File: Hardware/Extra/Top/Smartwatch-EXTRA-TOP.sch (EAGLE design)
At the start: 72 parts, among them U1 NRF52832_MODULE_MDBT42, U3 FT231XS, U4 PHOTOTRANSISTOR, U5 MCP9808-MSOP8

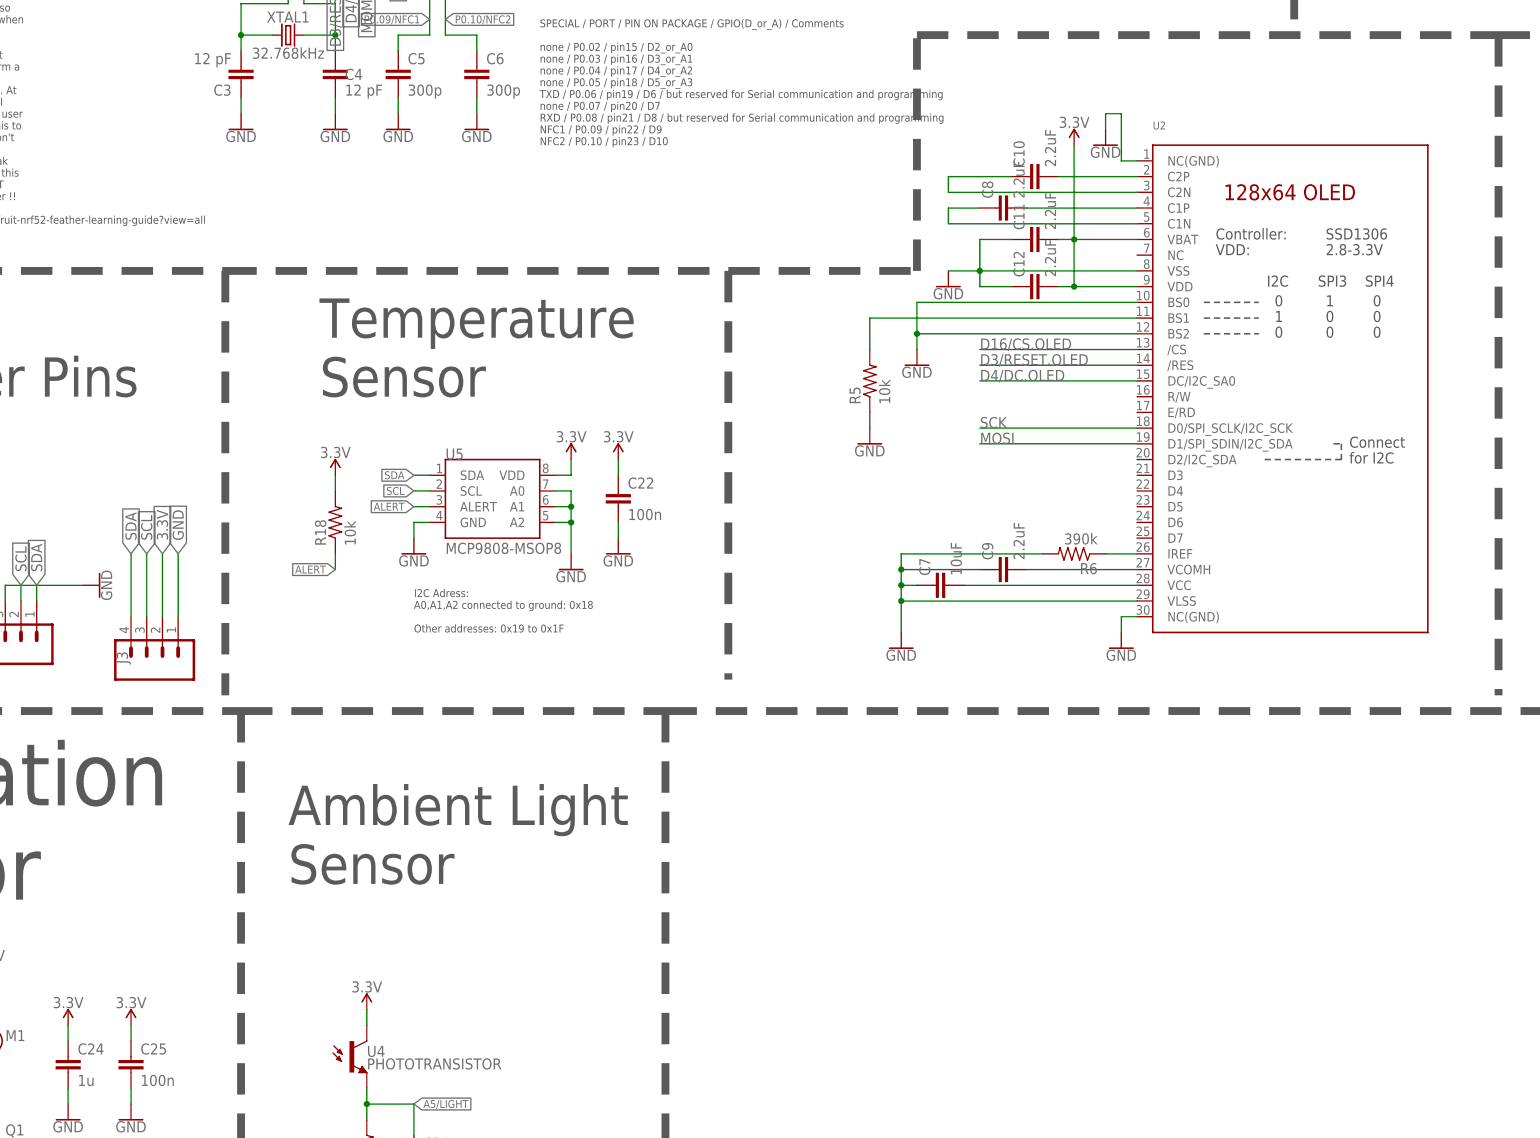
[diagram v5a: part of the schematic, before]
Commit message: Removed GPS, rearranged some other components
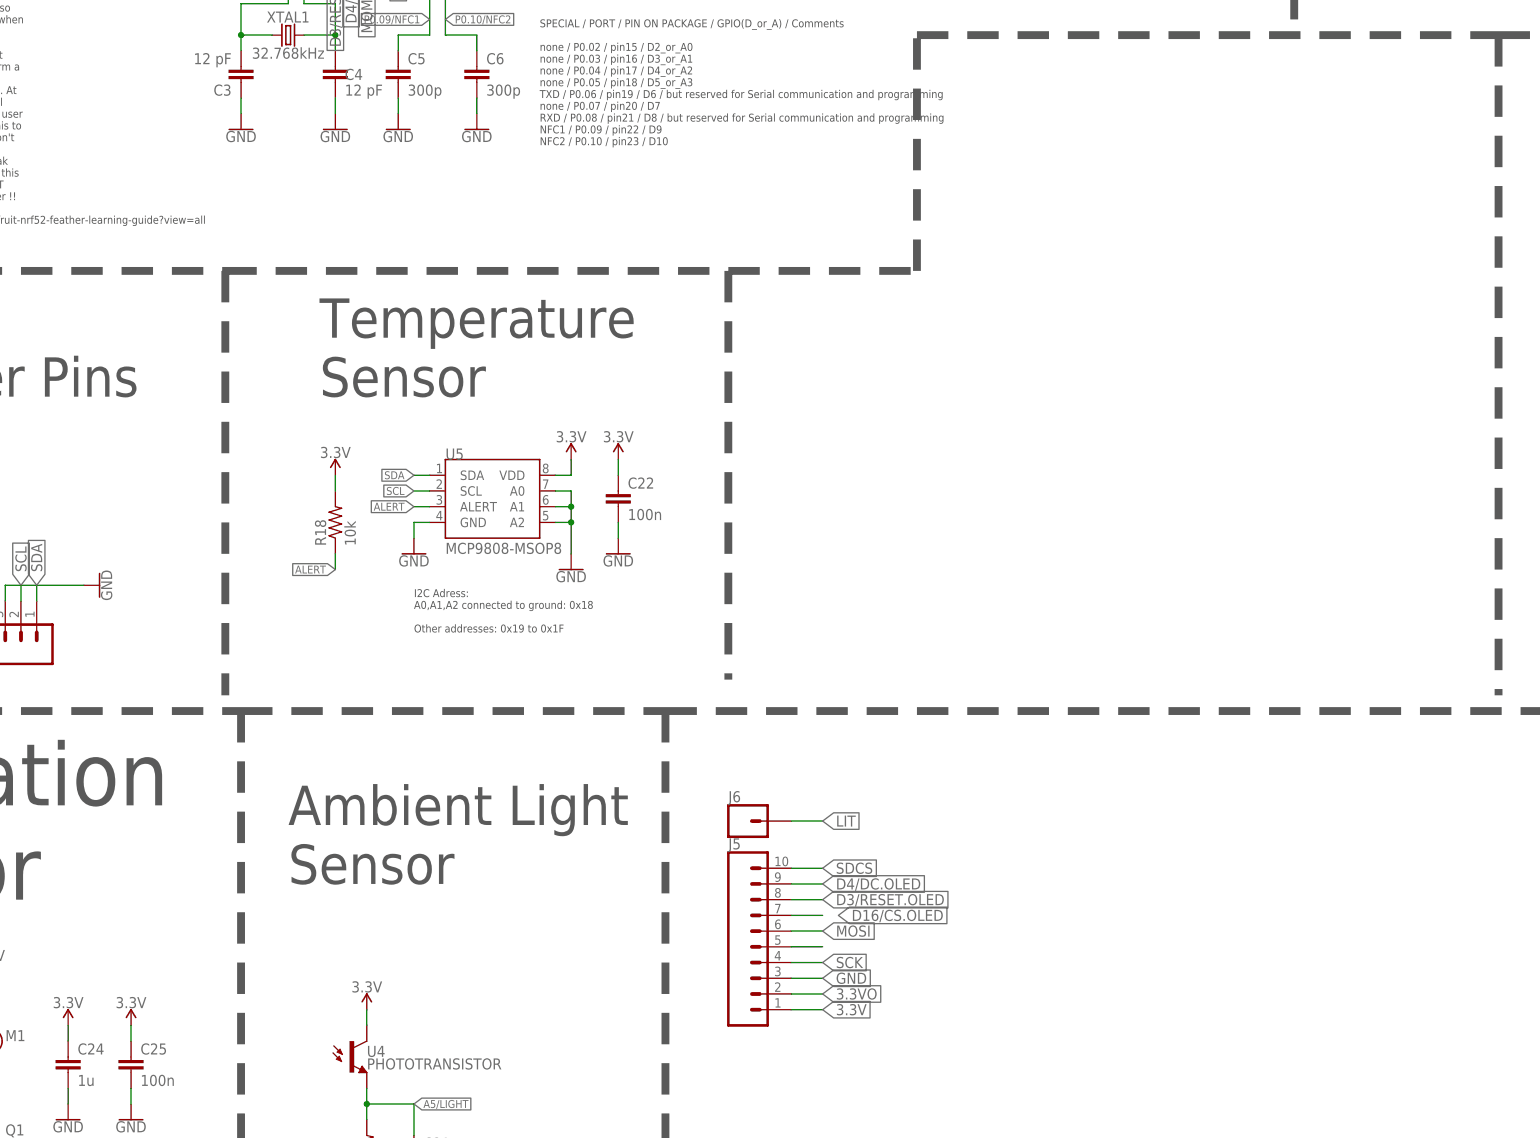
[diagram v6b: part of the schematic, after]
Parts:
- removed C10, C11, C12, C8, C9: 2.2uF, LinnesLab-Passives:CAPACITOR0402
- removed C7: 10uF, LinnesLab-Passives:CAPACITOR0603
- removed J3: (no value), LinnesLab-Connectors:CONN_041.27MM
- removed R5: 10k, LinnesLab-Passives:RESISTOR0603
- removed R6: 390k, LinnesLab-Passives:RESISTOR0603
- removed U2: (no value), LinnesLab-Displays:DISP_OLED_UG-2864HSWEG01-NO-WRAPAROUND
- added J5: (no value), LinnesLab-Connectors:CONN_10
- added J6: (no value), LinnesLab-Connectors:CONN_01
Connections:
- removed net N$1: R5.2, U2.BS1
- removed net N$13: C7.2, U2.VCC
- removed net N$15: C9.2, U2.VCOMH
- removed net N$2: R6.1, U2.IREF
- removed net N$3: C10.2, U2.C2P
- removed net N$5: C10.1, U2.C2N
- removed net N$7: C8.2, U2.C1P
- removed net N$8: C8.1, U2.C1N
- new net 3: J5.5
- new net 3.3VO: J5.2
- new net LIT: J6.1
- new net SDCS: J5.10
- net 3.3V: now also J5.1; no longer C11.2, C12.2, J3.2, U2.VBAT, U2.VDD
- net D16/CS.OLED: now also J5.7; no longer U2./CS
- net D3/RESET.OLED: now also J5.8; no longer U2./RES
- net D4/DC.OLED: now also J5.9; no longer U2.DC/I2C_SA0
- net GND: now also J5.3; no longer C11.1, C12.1, C7.1, C9.1, J3.1, R5.1, R6.2, U2.BS0, U2.BS2, U2.NC(GND)@1, U2.NC(GND)@2, U2.VLSS, U2.VSS
- net MOSI: now also J5.6; no longer U2.D1/SPI_SDIN/I2C_SDA
- net SCK: now also J5.4; no longer U2.D0/SPI_SCLK/I2C_SCK
- net SCL: no longer J3.3
- net SDA: no longer J3.4
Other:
- note removed: "OLED"

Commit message: GPS Removed, added back original display, kept pads for adafruit display
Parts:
- removed C24: 1u, LinnesLab-Passives:CAPACITOR0603
- removed C25: 100n, LinnesLab-Passives:CAPACITOR0603
- added C10: 100nF, LinnesLab-Passives:CAPACITOR0603
- added C11, C8: 1uF, LinnesLab-Passives:CAPACITOR0603
- added C12: 4.7uF, LinnesLab-Passives:CAPACITOR0603
- added C7, C9: 47pF, LinnesLab-Passives:CAPACITOR0603
- added R20: 10k, LinnesLab-Passives:RESISTOR0603
- added R21: 390k, LinnesLab-Passives:RESISTOR0603
- added U6: (no value), LinnesLab-Displays:DISP_OLED_UG-2864HSWEG01-NO-WRAPAROUND
- C1, C16: value 1u -> 1uF
- C13: value 100n -> 2.2uF
- C14: value 4.7u -> 100nF
- C15: value 47p -> 10pF
- C17: value 47p -> 100nF
- C18, C22: value 100n -> 2.2uF; device LinnesLab-Passives:CAPACITOR0603 -> LinnesLab-Passives:CAPACITOR0402
- C19: value 1u -> 2.2uF; device LinnesLab-Passives:CAPACITOR0603 -> LinnesLab-Passives:CAPACITOR0402
- C20: value 4.7u -> 10uF
- C21: device LinnesLab-Passives:CAPACITOR0603 -> LinnesLab-Passives:CAPACITOR0402
- C23: value 10pF -> 2.2uF; device LinnesLab-Passives:CAPACITOR0603 -> LinnesLab-Passives:CAPACITOR0402
- C5: value 300p -> 100nF
- C6: value 300p -> 4.7uF
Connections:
- removed net LIT: J6.1
- removed net P0.10/NFC2: C6.1, U1.P0.10
- new net D10/LIT: J6.1, U1.P0.10
- new net N$13: C18.1, U6.C2N
- new net N$15: C19.2, U6.C1P
- new net N$17: C19.1, U6.C1N
- new net N$19: C20.2, U6.VCC
- new net N$20: C22.2, U6.VCOMH
- new net N$5: R20.2, U6.BS1
- new net N$7: R21.1, U6.IREF
- new net N$8: C18.2, U6.C2P
- net 3.3V: now also C10.2, C11.1, C14.1, C15.2, C16.1, C17.1, C21.2, U6.VBAT, U6.VDD; no longer C18.2, C19.1, C22.1, C24.1, C25.1
- net A5/LIGHT: now also C13.1; no longer C21.1
- net D16/CS.OLED: now also U6./CS
- net D3/RESET.OLED: now also U6./RES
- net D4/DC.OLED: now also U6.DC/I2C_SA0
- net DTR: now also C5.1; no longer C13.1
- net GND: now also C10.1, C11.2, C12.2, C13.2, C14.2, C16.2, C20.1, C21.1, C22.1, C23.1, C6.1, C7.1, C8.1, C9.2, R20.1, R21.2, U6.BS0, U6.BS2, U6.NC(GND)@1, U6.NC(GND)@2, U6.VLSS, U6.VSS; no longer C14.1, C15.1, C16.1, C18.1, C19.2, C20.2, C21.2, C22.2, C24.2, C25.2, C5.2, C6.2
- net MOSI: now also U6.D1/SPI_SDIN/I2C_SDA
- net N$18: now also C15.1; no longer C23.1
- net P0.09/NFC1: no longer C5.1
- net RESET: now also C5.2; no longer C13.2
- net SCK: now also U6.D0/SPI_SCLK/I2C_SCK
- net USB+: now also C9.1; no longer C17.1
- net USB-: now also C7.2; no longer C15.2
- net VIN: now also C6.2, C8.2; no longer C14.2, C16.2
- net VLIPO: now also C12.1; no longer C20.1
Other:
- note added: "OLED"
- moved on the sheet: C13, C14, C15, C16, C17, C18, C19, C20, C21, C22, C23, C5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
